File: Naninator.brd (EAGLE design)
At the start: 43.2 x 17.8 mm, 26 parts, among them J001 USB_MICROB_JST, J002 M15, J003 M15, U001 FT232RLSSOP, U401 ATMEGA328P, Y401 16MHz

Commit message: Rescued from Osaka working copy
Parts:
- removed U$2: (no value), SparkFun-Aesthetics:OSHW-LOGO-L
- added JP1, JP2: (no value), SparkFun-Connectors:1X03
- D003: value DIODE-SCHOTTKY_ -> (none); device SparkFun-DiscreteSemi:SMA-DIODE -> SparkFun-DiscreteSemi:SOD-323
- moved D003 3.21 mm to (6.60, 6.60), turned to 270 degrees
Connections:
- net D11: now also JP2.2
- net D12: now also JP1.1
- net D13: now also JP1.2
- net GND: now also JP2.1
- net RESET: now also JP1.3
- net VBUS: now also D003.2; no longer D003.A
- net VCC: now also D003.1, JP2.3; no longer D003.C
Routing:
- net VCC: track 77.0 -> 0.00 mm, vias 7 -> 0
- net D13: track 49.4 -> 0.00 mm, vias 4 -> 0
- net D0: track 45.3 -> 0.00 mm, vias 2 -> 0
- net RESET: track 42.7 -> 0.00 mm, vias 5 -> 0
- net VBUS: track 37.0 -> 0.00 mm, vias 2 -> 0
- net D1: track 36.6 -> 0.00 mm, vias 3 -> 0
- net D10: track 34.0 -> 0.00 mm, vias 4 -> 0
- net D3: track 31.2 -> 0.00 mm, vias 3 -> 0
- net D4: track 28.2 -> 0.00 mm, vias 2 -> 0
- net D12: track 26.5 -> 0.00 mm, vias 2 -> 0
- net D11: track 24.1 -> 0.00 mm, vias 2 -> 0
- net AREF: track 21.1 -> 0.00 mm, vias 3 -> 0
- net D9: track 20.4 -> 0.00 mm, vias 2 -> 0
- net D8: track 16.3 -> 0.00 mm, vias 4 -> 0
- net D7: track 15.7 -> 0.00 mm, vias 2 -> 0
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- removed copper zone on layer 1, net GND
- removed copper zone on layer 16, net GND

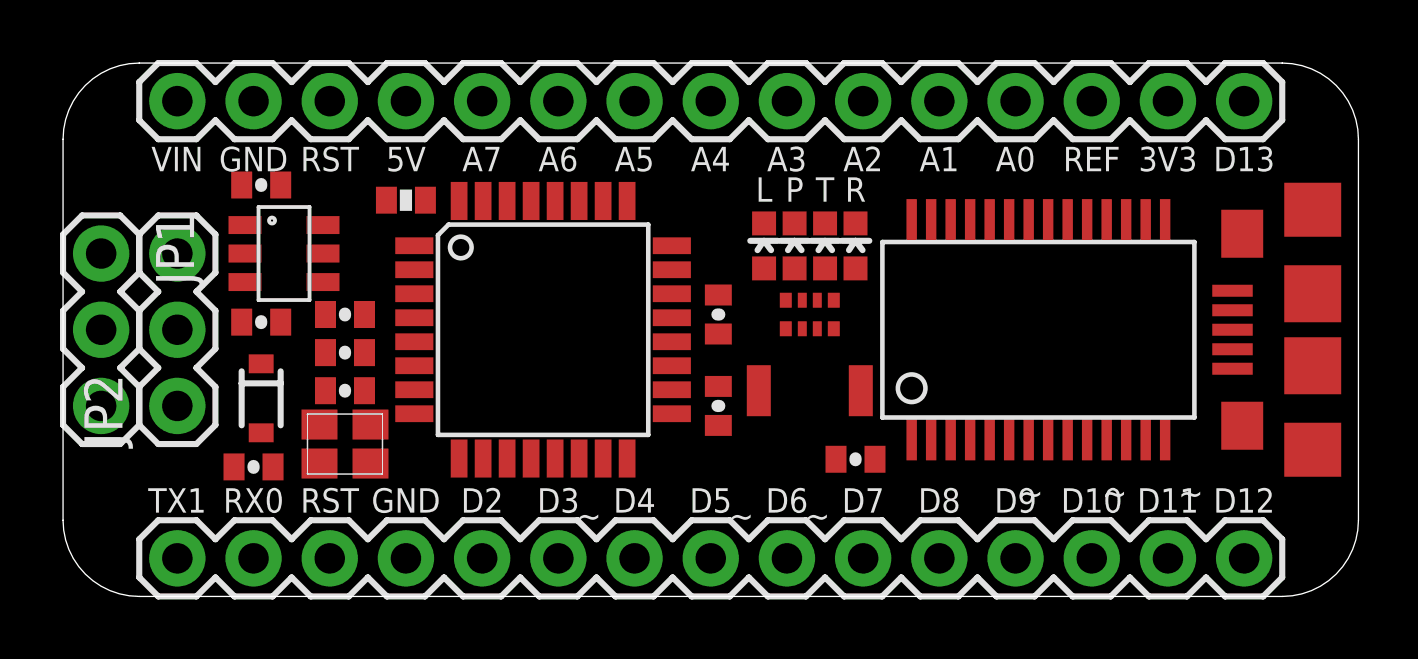
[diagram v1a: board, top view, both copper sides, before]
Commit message: Naninator with regulator on top side, some .gitignore fixes
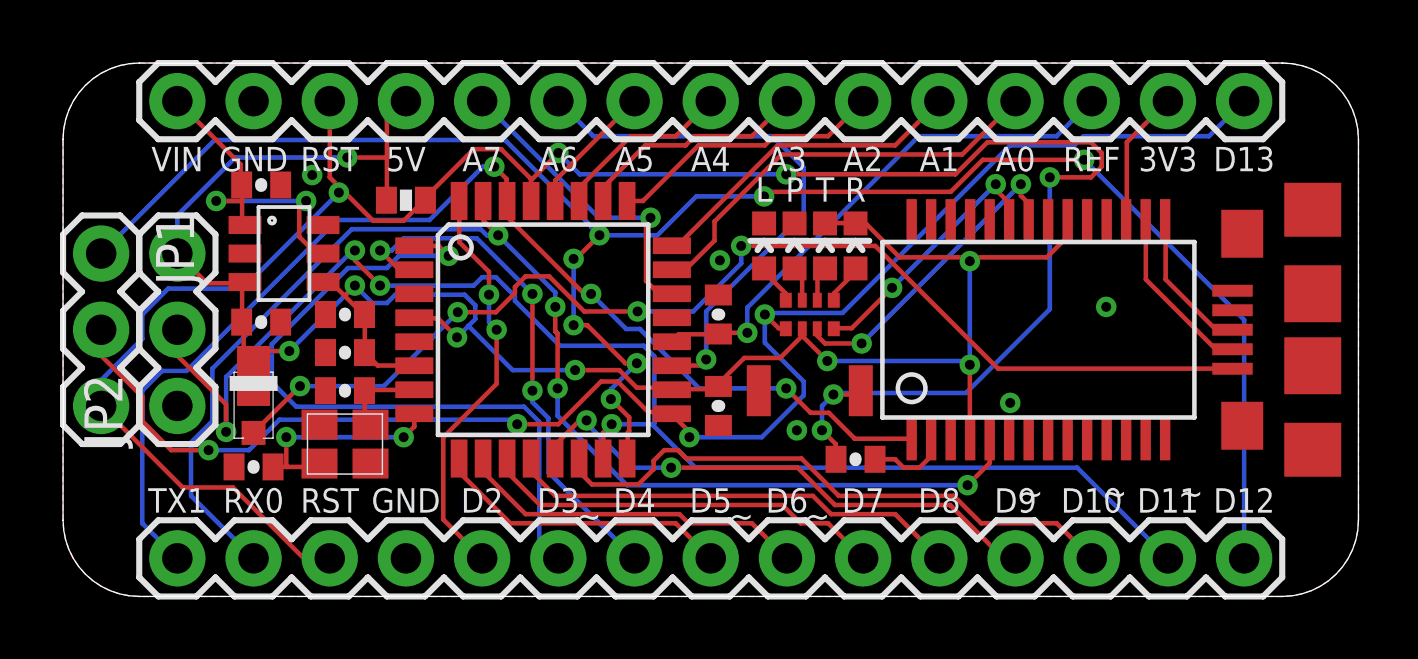
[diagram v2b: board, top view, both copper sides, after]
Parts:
- added U$2: (no value), SparkFun-Aesthetics:OSHW-LOGO-L
- D003: value (none) -> MSS1P6; device SparkFun-DiscreteSemi:SOD-323 -> KwanSystems:MICROSMP
- moved D003 0.36 mm to (6.35, 6.35)
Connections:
- net VBUS: now also D003.A; no longer D003.2
- net VCC: now also D003.K; no longer D003.1
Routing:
- net RESET: track 0.00 -> 72.6 mm, vias 0 -> 6
- net VCC: track 0.00 -> 71.6 mm, vias 0 -> 8
- net D12: track 0.00 -> 62.1 mm, vias 0 -> 7
- net D13: track 0.00 -> 51.6 mm, vias 0 -> 4
- net D11: track 0.00 -> 47.9 mm, vias 0 -> 4
- net D1: track 0.00 -> 43.7 mm, vias 0 -> 4
- net D0: track 0.00 -> 39.3 mm, vias 0 -> 3
- net VBUS: track 0.00 -> 38.3 mm, vias 0 -> 4
- net D3: track 0.00 -> 23.9 mm, vias 0 -> 1
- net D10: track 0.00 -> 19.8 mm
- net D9: track 0.00 -> 18.1 mm, vias 0 -> 2
- net A6: track 0.00 -> 18.1 mm, vias 0 -> 1
- net AREF: track 0.00 -> 17.8 mm, vias 0 -> 1
- net D4: track 0.00 -> 17.7 mm, vias 0 -> 3
- net D8: track 0.00 -> 15.3 mm
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- added copper zone on layer 1, net GND
- added copper zone on layer 16, net GND

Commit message: Digikey part numbers for Naninator. Added the MicroSMP diode to eagle3d.
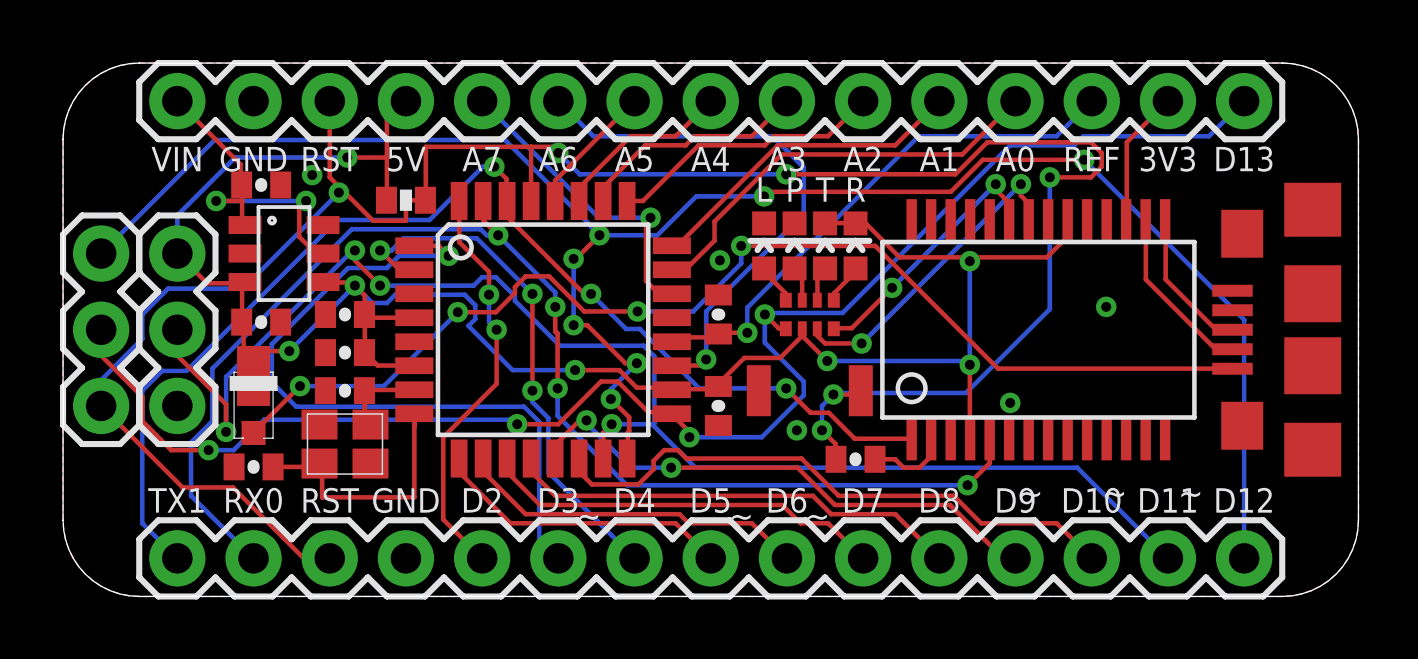
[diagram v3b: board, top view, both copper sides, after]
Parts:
- D001: value blue -> BLUE
- D002: value red -> RED
- D401: value green -> GREEN
- D402: value amber -> YELLOW
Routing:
- net RESET: track 72.6 -> 74.5 mm
- net N$2: track 7.42 -> 9.05 mm, vias 2 -> 0
- net VCC: vias 8 -> 7

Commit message: Merged Mio's KwanSystems.lbr, updated all eagle files to use it.
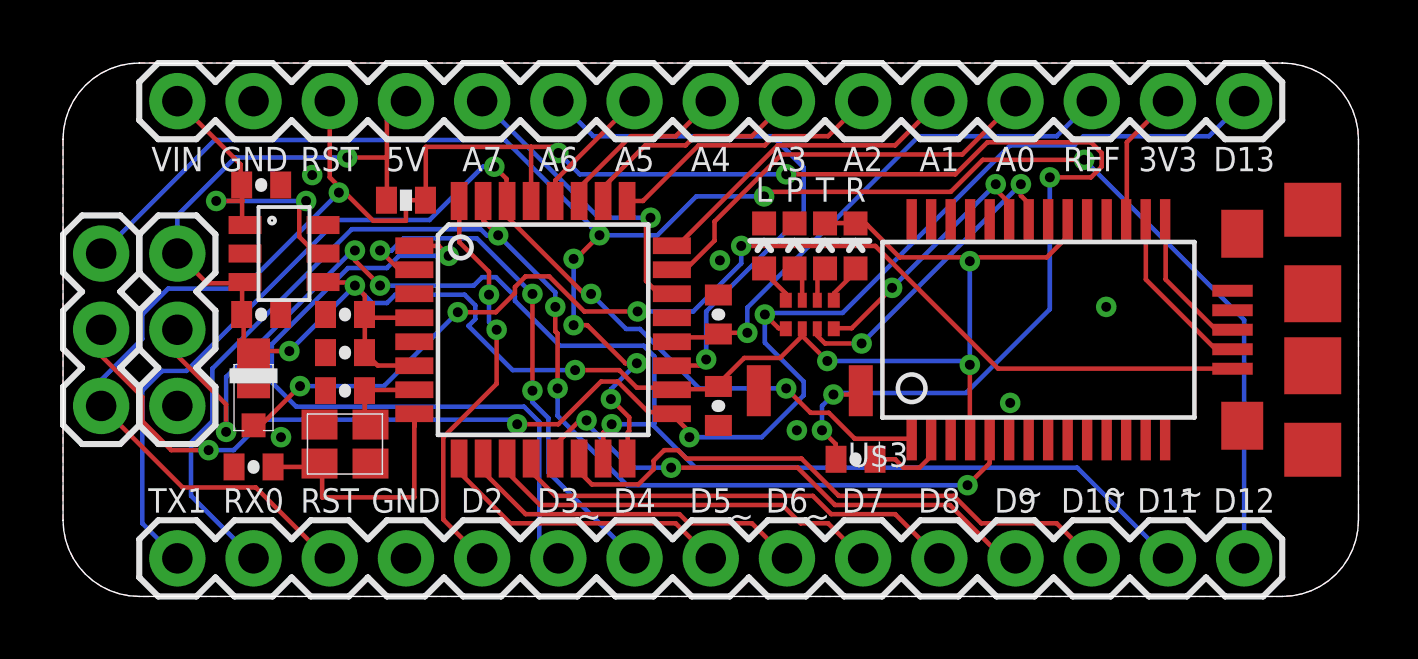
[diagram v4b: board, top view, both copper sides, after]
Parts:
- U$3: value (none) -> B3U-1000P
- moved D003 0.25 mm to (6.35, 6.60)
- moved C203 0.25 mm to (6.60, 9.40)
- renumbered S429 to U$3
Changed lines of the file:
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@@
 <setting verticaltext="up"/>
 </settings>
-<grid distance="10" unitdist="mil" unit="mil" style="lines" multiple="1" display="yes" altdistance="0.025" altunitdist="inch" altunit="inch"/>
+<grid distance="1" unitdist="mil" unit="mil" style="lines" multiple="1" display="yes" altdistance="0.025" altunitdist="inch" altunit="inch"/>
 <layers>
 <layer number="1" name="Top" color="4" fill="1" visible="yes" active="yes"/>
@@
 <layer number="19" name="Unrouted" color="13" fill="1" visible="yes" active="yes"/>
 <layer number="20" name="Dimension" color="15" fill="1" visible="yes" active="yes"/>
-<layer number="21" name="tPlace" color="15" fill="1" visible="yes" active="yes"/>
+<layer number="21" name="tPlace" color="15" fill="1" visible="no" active="yes"/>
 <layer number="22" name="bPlace" color="7" fill="1" visible="no" active="yes"/>
-<layer number="23" name="tOrigins" color="15" fill="1" visible="no" active="yes"/>
-<layer number="24" name="bOrigins" color="15" fill="1" visible="no" active="yes"/>
+<layer number="23" name="tOrigins" color="15" fill="1" visible="yes" active="yes"/>
+<layer number="24" name="bOrigins" color="15" fill="1" visible="yes" active="yes"/>
 <layer number="25" name="tNames" color="13" fill="1" visible="yes" active="yes"/>
 <layer number="26" name="bNames" color="13" fill="1" visible="yes" active="yes"/>
@@
 <attribute name="DIGIKEY" value="478-6955-1-ND" x="9.398" y="5.08" size="1.778" layer="27" display="off"/>
 </element>
-<element name="S429" library="KwanSystems" package="B3U-1000P" value="" x="24.892" y="6.858" smashed="yes">
-<attribute name="DIGIKEY" value="SW1020CT-ND" x="24.892" y="6.858" size="1.778" layer="27" display="off"/>
-</element>
 <element name="U201" library="KwanSystems" package="SOT-23-6" value="" x="7.366" y="11.43" smashed="yes" rot="R270">
 <attribute name="NAME" x="7.166" y="12.79" size="0.8128" layer="51" rot="R270"/>
@@
 <attribute name="DIGIKEY" value="MAX8881EUT50+TCT-ND" x="7.366" y="11.43" size="1.778" layer="27" rot="R270" display="off"/>
 </element>
-<element name="C203" library="SparkFun" package="0402-CAP" value="4.7uF" x="6.604" y="9.144" smashed="yes">
-<attribute name="NAME" x="7.239" y="8.8265" size="0.4064" layer="51"/>
-<attribute name="VALUE" x="5.5245" y="8.001" size="0.4064" layer="27"/>
-<attribute name="DIGIKEY" value="445-7395-1-ND" x="6.604" y="9.144" size="1.778" layer="27" display="off"/>
+<element name="C203" library="SparkFun" package="0402-CAP" value="4.7uF" x="6.604" y="9.398" smashed="yes">
+<attribute name="NAME" x="7.239" y="9.0805" size="0.4064" layer="51"/>
+<attribute name="VALUE" x="5.5245" y="8.255" size="0.4064" layer="27"/>
+<attribute name="DIGIKEY" value="445-7395-1-ND" x="6.604" y="9.398" size="1.778" layer="27" display="off"/>
 </element>
 <element name="C201" library="SparkFun" package="0402-CAP" value="1uF" x="6.604" y="13.716" smashed="yes">
@@
 <attribute name="DIGIKEY" value="445-1415-1-ND" x="6.604" y="13.716" size="1.778" layer="27" display="off"/>
 </element>
-<element name="D003" library="KwanSystems" package="MICROSMP" value="MSS1P6" x="6.35" y="6.35" smashed="yes" rot="R270">
-<attribute name="NAME" x="4.445" y="6.604" size="0.4064" layer="51" rot="R270"/>
-<attribute name="VALUE" x="8.001" y="6.096" size="0.4064" layer="27" rot="R270"/>
-<attribute name="DIGIKEY" value="MSS1P6-M3/89AGICT-ND" x="6.35" y="6.35" size="1.778" layer="27" rot="R270" display="off"/>
+<element name="D003" library="KwanSystems" package="MICROSMP" value="MSS1P6" x="6.35" y="6.604" smashed="yes" rot="R270">
+<attribute name="NAME" x="4.445" y="6.858" size="0.4064" layer="51" rot="R270"/>
+<attribute name="VALUE" x="8.001" y="6.35" size="0.4064" layer="27" rot="R270"/>
+<attribute name="DIGIKEY" value="MSS1P6-M3/89AGICT-ND" x="6.35" y="6.604" size="1.778" layer="27" rot="R270" display="off"/>
 </element>
 <element name="U$1" library="KwanSystems" package="KWAN_CIRCLE" value="" x="38.1" y="8.89" rot="MR0"/>
@@
 </element>
 <element name="U$2" library="SparkFun-Aesthetics" package="OSHW-LOGO-L" value="" x="10.16" y="8.89" rot="MR0"/>
+<element name="U$3" library="KwanSystems" package="B3U-1000P" value="B3U-1000P" x="24.892" y="6.858"/>
 </elements>
 <signals>
@@
 <wire x1="5.969" y1="10.3886" x2="5.969" y2="9.144" width="0.1524" layer="1"/>
 <wire x1="6.0452" y1="10.4648" x2="5.969" y2="10.3886" width="0.1524" layer="1"/>
-<wire x1="5.969" y1="9.144" x2="5.954" y2="9.144" width="0.1524" layer="1"/>
+<wire x1="5.969" y1="9.144" x2="5.954" y2="9.398" width="0.1524" layer="1"/>
 <wire x1="6.0452" y1="10.4648" x2="6.066" y2="10.48" width="0.1524" layer="1"/>
 <wire x1="6.0198" y1="7.6962" x2="6.0198" y2="9.0932" width="0.1524" layer="1"/>
 <wire x1="6.35" y1="7.366" x2="6.0198" y2="7.6962" width="0.1524" layer="1"/>
-<wire x1="6.0198" y1="9.0932" x2="5.954" y2="9.144" width="0.1524" layer="1"/>
-<wire x1="6.35" y1="7.366" x2="6.35" y2="7.35" width="0.1524" layer="1"/>
+<wire x1="6.0198" y1="9.0932" x2="5.954" y2="9.398" width="0.1524" layer="1"/>
+<wire x1="6.35" y1="7.366" x2="6.35" y2="7.604" width="0.1524" layer="1"/>
 <wire x1="4.8006" y1="10.4394" x2="5.9182" y2="10.4394" width="0.1524" layer="1"/>
 <wire x1="3.81" y1="11.43" x2="4.8006" y2="10.4394" width="0.1524" layer="1"/>
@@
 <wire x1="7.5438" y1="8.1788" x2="9.7282" y2="10.3632" width="0.1524" layer="16"/>
 <wire x1="6.0706" y1="8.1788" x2="7.5438" y2="8.1788" width="0.1524" layer="1"/>
-<wire x1="6.0706" y1="8.1788" x2="6.35" y2="7.35" width="0.1524" layer="1"/>
+<wire x1="6.0706" y1="8.1788" x2="6.35" y2="7.604" width="0.1524" layer="1"/>
 <wire x1="9.4742" y1="14.6304" x2="10.795" y2="14.6304" width="0.1524" layer="1"/>
 <wire x1="5.7404" y1="14.6304" x2="9.4742" y2="14.6304" width="0.1524" layer="16"/>
@@
 <wire x1="9.906" y1="9.398" x2="10.16" y2="9.398" width="0.1524" layer="1"/>
 </signal>
-<signal name="GND" airwireshidden="yes">
+<signal name="GND">
 <contactref element="C404" pad="2"/>
 <contactref element="C406" pad="2"/>
@@
 <contactref element="Y401" pad="2" route="any" routetag="1"/>
 <contactref element="Y401" pad="4" route="any" routetag="1"/>
-<contactref element="S429" pad="P$1"/>
 <contactref element="C201" pad="2"/>
 <contactref element="C203" pad="2"/>
@@
 <vertex x="0" y="15.24" curve="-90"/>
 </polygon>
-<wire x1="3.81" y1="6.35" x2="5.7" y2="4.318" width="0" layer="19" extent="1-1"/>
+<contactref element="U$3" pad="P$1"/>
+<via x="7.2644" y="5.3086" extent="1-16" drill="0.3302"/>
 </signal>
 <signal name="N$1">
@@
 <contactref element="R429" pad="2"/>
 <contactref element="J003" pad="13"/>
-<contactref element="S429" pad="P$2"/>
 <contactref element="JP1" pad="3"/>
-<wire x1="8.0264" y1="1.27" x2="8.89" y2="1.27" width="0.1524" layer="1"/>
-<wire x1="5.6642" y1="3.6322" x2="8.0264" y2="1.27" width="0.1524" layer="1"/>
-<wire x1="3.9878" y1="3.6322" x2="5.6642" y2="3.6322" width="0.1524" layer="1"/>
+<wire x1="8.7884" y1="1.27" x2="8.89" y2="1.27" width="0.1524" layer="1"/>
+<wire x1="6.4262" y1="3.6322" x2="8.7884" y2="1.27" width="0.1524" layer="1"/>
+<wire x1="3.9878" y1="3.6322" x2="6.4262" y2="3.6322" width="0.1524" layer="1"/>
 <wire x1="1.27" y1="6.35" x2="3.9878" y2="3.6322" width="0.1524" layer="1"/>
 <wire x1="25.7556" y1="5.08" x2="25.7556" y2="4.572" width="0.1524" layer="1"/>
@@
 <wire x1="26.5684" y1="6.858" x2="26.4414" y2="6.731" width="0.1524" layer="1"/>
 <wire x1="25.7556" y1="4.572" x2="25.766" y2="4.572" width="0.1524" layer="1"/>
-<wire x1="26.5684" y1="6.858" x2="26.592" y2="6.858" width="0.1524" layer="1"/>
 <wire x1="12.0904" y1="13.208" x2="12.08" y2="13.208" width="0.1524" layer="1"/>
 <wire x1="15.5956" y1="13.1826" x2="15.602" y2="13.1826" width="0.1524" layer="1"/>
@@
 <wire x1="12.0142" y1="13.208" x2="11.43" y2="13.208" width="0.1524" layer="1"/>
 <wire x1="11.43" y1="13.208" x2="11.43" y2="12.5222" width="0.1524" layer="1"/>
+<contactref element="U$3" pad="P$2"/>
+<wire x1="26.5684" y1="6.858" x2="26.592" y2="6.858" width="0.4064" layer="1"/>
 </signal>
 <signal name="3V3">
@@
 <wire x1="31.1658" y1="7.5946" x2="27.0764" y2="11.684" width="0.1524" layer="1"/>
 <wire x1="38.9636" y1="7.5946" x2="31.1658" y2="7.5946" width="0.1524" layer="1"/>
-<wire x1="6.35" y1="5.461" x2="6.35" y2="5.45" width="0.1524" layer="1"/>
+<wire x1="6.35" y1="5.461" x2="6.35" y2="5.704" width="0.1524" layer="1"/>
 <wire x1="38.9636" y1="7.5946" x2="38.981" y2="7.59" width="0.1524" layer="1"/>
 <via x="7.8994" y="7.0104" extent="1-16" drill="0.3302"/>

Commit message: Rocketometer6050 fully routed, almost fully manually
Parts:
- U$2: device SparkFun-Aesthetics:OSHW-LOGO-L -> SparkFun-Aesthetics:OSHW-LOGO-S
- moved U$2 2.03 mm to (10.2, 6.86)
- renumbered D001 to D022, D002 to D023, U$3 to S429
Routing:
- net N$4: track 5.83 -> 7.19 mm
- net N$3: track 4.91 -> 5.89 mm
- net VCC: track 72.0 -> 72.9 mm
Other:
- board text added: "19 Nov 2012"
- board text removed: "9 Oct 2012"
